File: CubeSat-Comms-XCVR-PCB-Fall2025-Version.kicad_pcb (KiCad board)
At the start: 4 copper layers, 93.9 x 97.3 mm, 68 parts, among them J1 Screw_Terminal_01x02, J2 Screw_Terminal_01x02, J3 Conn_Coaxial, J4 Conn_01x12_Pin, U1 CC1101RGP, U2 SKY65366-21, U3 PE4251MLI-Z, U4 NCP186AMX390TAG, Y1 NX3225GA-26MHZ-TI

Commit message: edits
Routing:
- net RF_N: track 0.00 -> 12.8 mm
- net Net-(C10-Pad2): track 2.52 -> 5.02 mm
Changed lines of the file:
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@@
+	)
+	(segment
+		(start 79.385 92.75)
+		(end 79.1976 92.5626)
+		(width 0.2)
+		(layer "F.Cu")
+		(net 3)
+	)
+	(segment
+		(start 79.385 92.75)
+		(end 82.053 92.75)
+		(width 0.2)
+		(layer "F.Cu")
+		(net 3)
+	)
+	(segment
+		(start 79.1976 92.5626)
+		(end 69.29625 92.5626)
+		(width 0.2)
+		(layer "F.Cu")
+		(net 3)
+	)
+	(segment
+		(start 83.853 92.75)
+		(end 84.953 93.85)
+		(width 0.2)
+		(layer "F.Cu")
+		(net 4)
+	)
+	(segment
+		(start 82.917 92.75)
+		(end 83.853 92.75)
+		(width 0.2)
+		(layer "F.Cu")
+		(net 4)
 	)
 	(segment

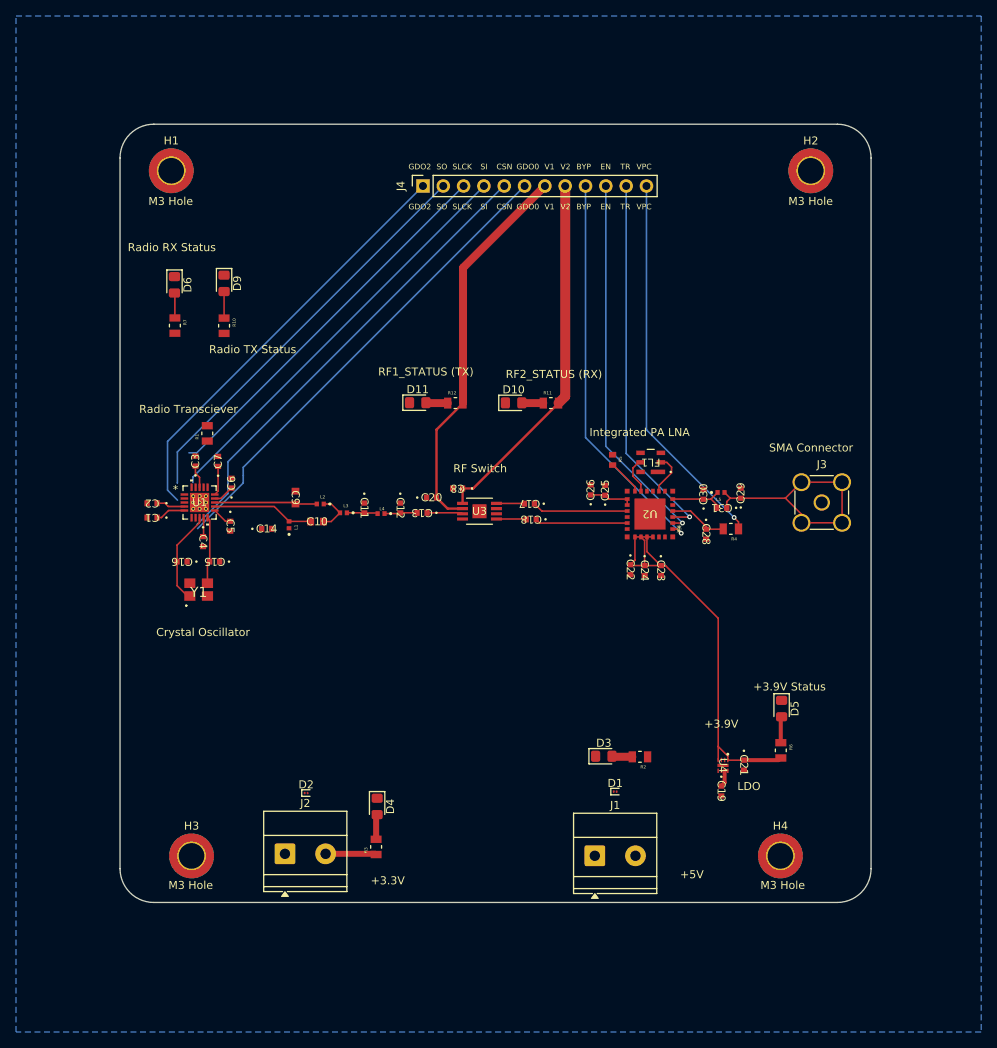
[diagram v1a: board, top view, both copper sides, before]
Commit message: revised TVS ESD protection diodes, added JST XH connectors for power
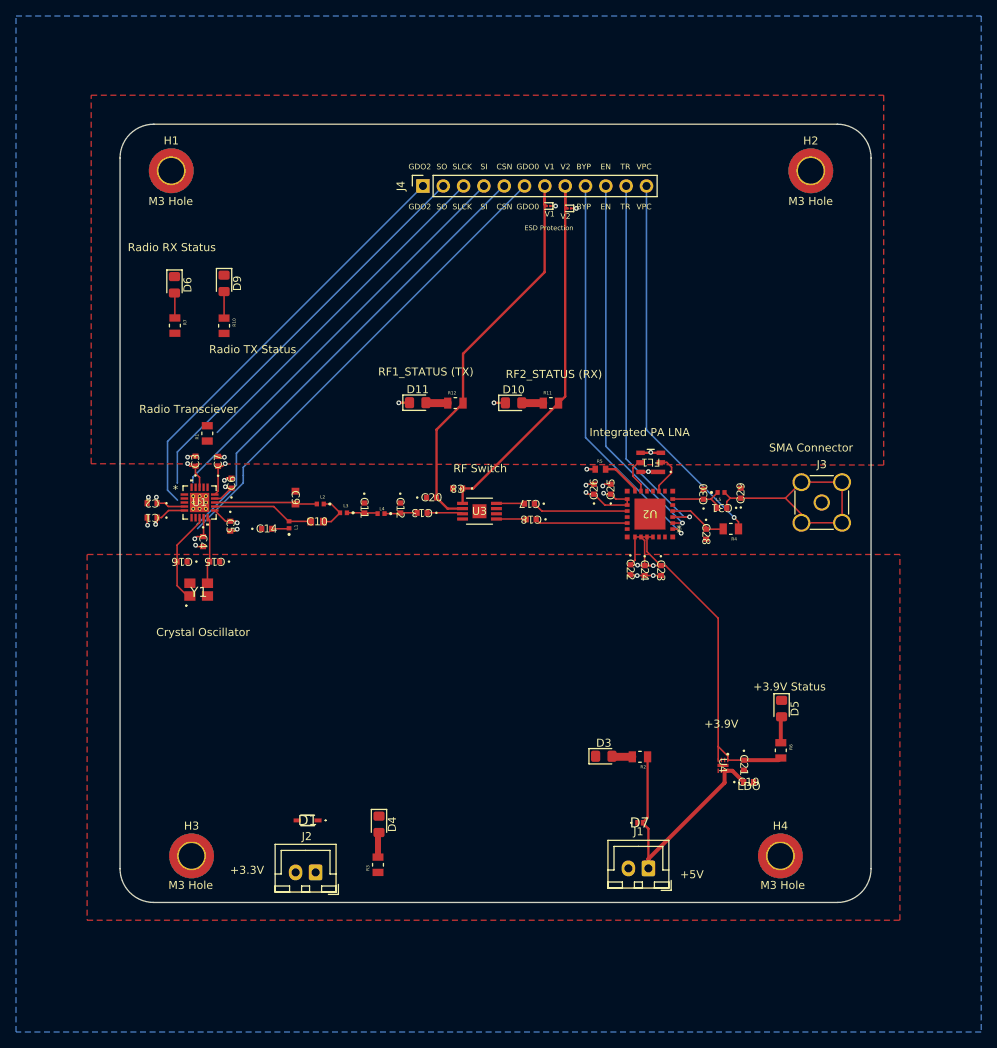
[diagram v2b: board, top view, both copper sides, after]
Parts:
- added D7: PESD5V5C1BL-QYL, comms-board-footprints-passives:PESD5V5C1BLQYL, F.Cu at (122.4, 132.6)
- added D8: ESD131-B1-W0201, Diode_SMD:Infineon_SG-WLL-2-3_0.58x0.28_P0.36mm, F.Cu at (113.6, 55.8)
- D1: value ESD131-B1-W0201 -> ESDS311DYFR; footprint Diode_SMD:Infineon_SG-WLL-2-3_0.58x0.28_P0.36mm -> comms-board-footprints-passives:ESDS311DYFR
- J1, J2: value Screw_Terminal_01x02 -> Conn_01x02_Pin; footprint TerminalBlock_Phoenix:TerminalBlock_Phoenix_MKDS-1,5-2-5.08_1x02_P5.08mm_Horizontal -> Connector_JST:JST_XH_B2B-XH-A_1x02_P2.50mm_Vertical
- moved D2 79.4 mm to (111.0, 55.5), turned to 180 degrees
- moved D1 38.6 mm to (80.9, 132.3), turned to 180 degrees
- moved J1 6.88 mm to (123.5, 138.3), turned to 180 degrees
- moved J2 4.48 mm to (81.9, 138.8), turned to 180 degrees
- moved C19 3.60 mm to (136.0, 127.5), turned to 0 degrees
- moved D4 2.25 mm to (89.8, 132.8)
- moved R3 2.25 mm to (89.7, 137.8)
- moved R5 1.92 mm to (117.5, 88.4), turned to 0 degrees
- moved C25 0.72 mm to (118.8, 90.9)
- moved C26 0.42 mm to (116.7, 90.9)
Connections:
- D1 pad 1: GND -> +3.3V
- D1 pad 2: +5V -> GND
- D2 pad 2: +3.3V -> V1
- J1 pad 1: GND -> +5V
- J1 pad 2: +5V -> GND
- J2 pad 1: GND -> +3.3V
- J2 pad 2: +3.3V -> GND
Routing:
- net +5V: track 2.88 -> 34.4 mm
- net GND: track 0.00 -> 22.6 mm, vias 0 -> 18
- net +3.3V: track 33.3 -> 38.0 mm, vias 0 -> 9
- net SCLK: track 48.2 -> 43.6 mm
- net V2: track 45.8 -> 48.7 mm
- net Net-(C14-Pad2): track 0.00 -> 2.21 mm
- net V1: track 48.4 -> 49.6 mm
- net +3.9V: track 54.4 -> 55.5 mm, vias 0 -> 2
- net Net-(U2-RBIAS): track 4.47 -> 5.00 mm
- added copper zone on F.Cu, net GND
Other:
- board text added: "ESD Protection"

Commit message: slight edit
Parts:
- moved R10 15.2 mm to (85.0, 66.0), turned to 0 degrees
- moved D9 9.29 mm to (79.7, 66.0), turned to 0 degrees
- moved R7 7.33 mm to (70.1, 66.0), turned to 0 degrees
- moved D6 1.04 mm to (65.0, 66.0), turned to 0 degrees
